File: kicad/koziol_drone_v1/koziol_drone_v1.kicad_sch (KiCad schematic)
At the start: 0 parts

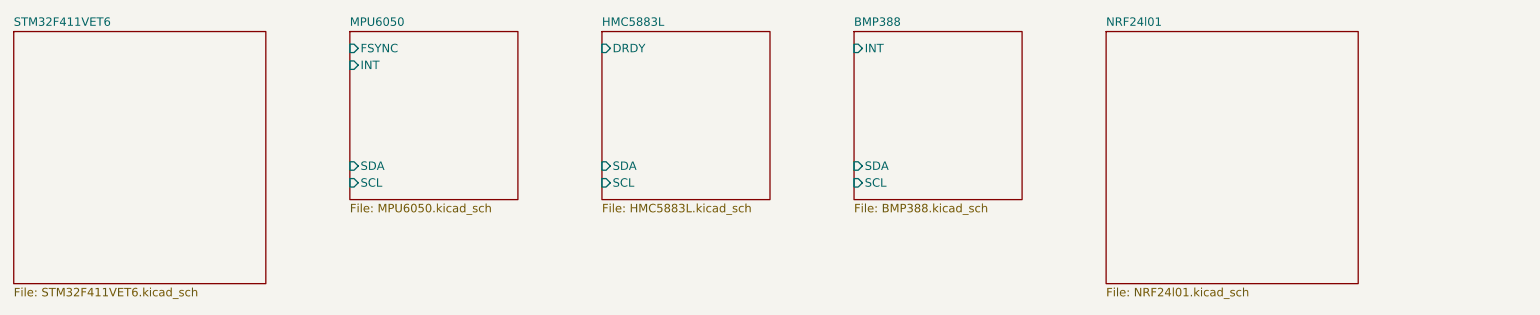
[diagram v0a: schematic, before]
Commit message: mcu scheme + buses
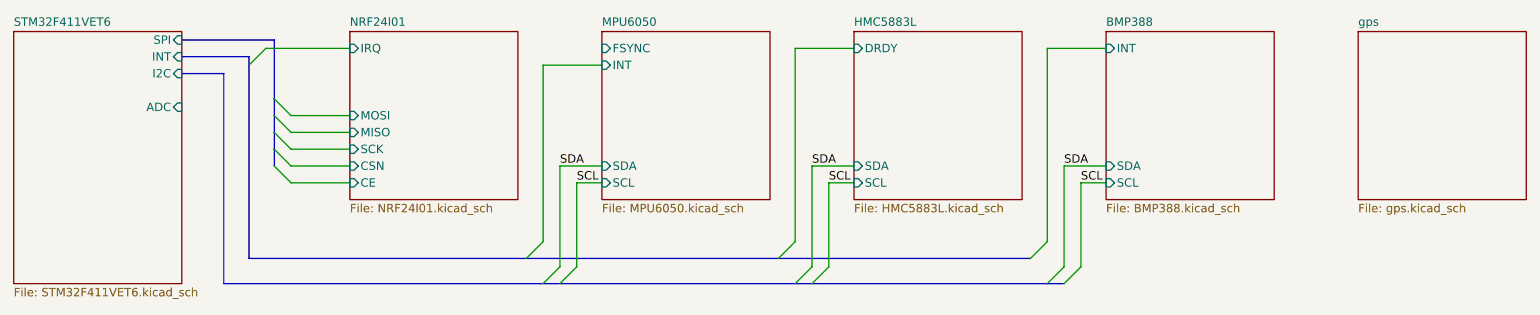
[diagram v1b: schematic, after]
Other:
- added sheet gps (gps.kicad_sch)
- sheet NRF24l01 ports: added CE, CSN, IRQ, MISO, MOSI, SCK; removed none
- sheet STM32F411VET6 ports: added ADC, I2C, INT, SPI; removed none

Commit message: scheme descriptions and PDF plot
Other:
- note added: "MAIN_koziol_drone"
- note added: "Main block scheme of sensor/communication peripheriesand communication buses between them and the MCU."
